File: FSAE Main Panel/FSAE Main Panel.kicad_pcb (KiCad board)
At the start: 2 copper layers, 164 x 83 mm, 244 parts, among them J1 Conn_01x08, J2 Conn_01x08, J3 Conn_01x10, J4 USB Micro B, J5 Cortex_Debug, J6 Conn_01x08, Q301 IRLML6402TRPBF, Q501 SI2308CDS-T1-GE3, Q502 SI2308CDS-T1-GE3, Q503 SI2308CDS-T1-GE3, Q504 SI2308CDS-T1-GE3, U101 SAMD21G18A-AU, U201 CD40106BPWR, U202 CD74HC238PWR, U301 TPS564201, U302 LM2940IMP-5.0/NOPB, U303 LP5907MFX-3.3, U304 LP5907MFX-3.3, U305 LP5907MFX-3.3, U401 MCP25625, U501 TLC6C598, U502 TLC6C5816, U503 TLC6C5816, Y101 32.768kHz, Y102 16MHz, Y401 16MHz

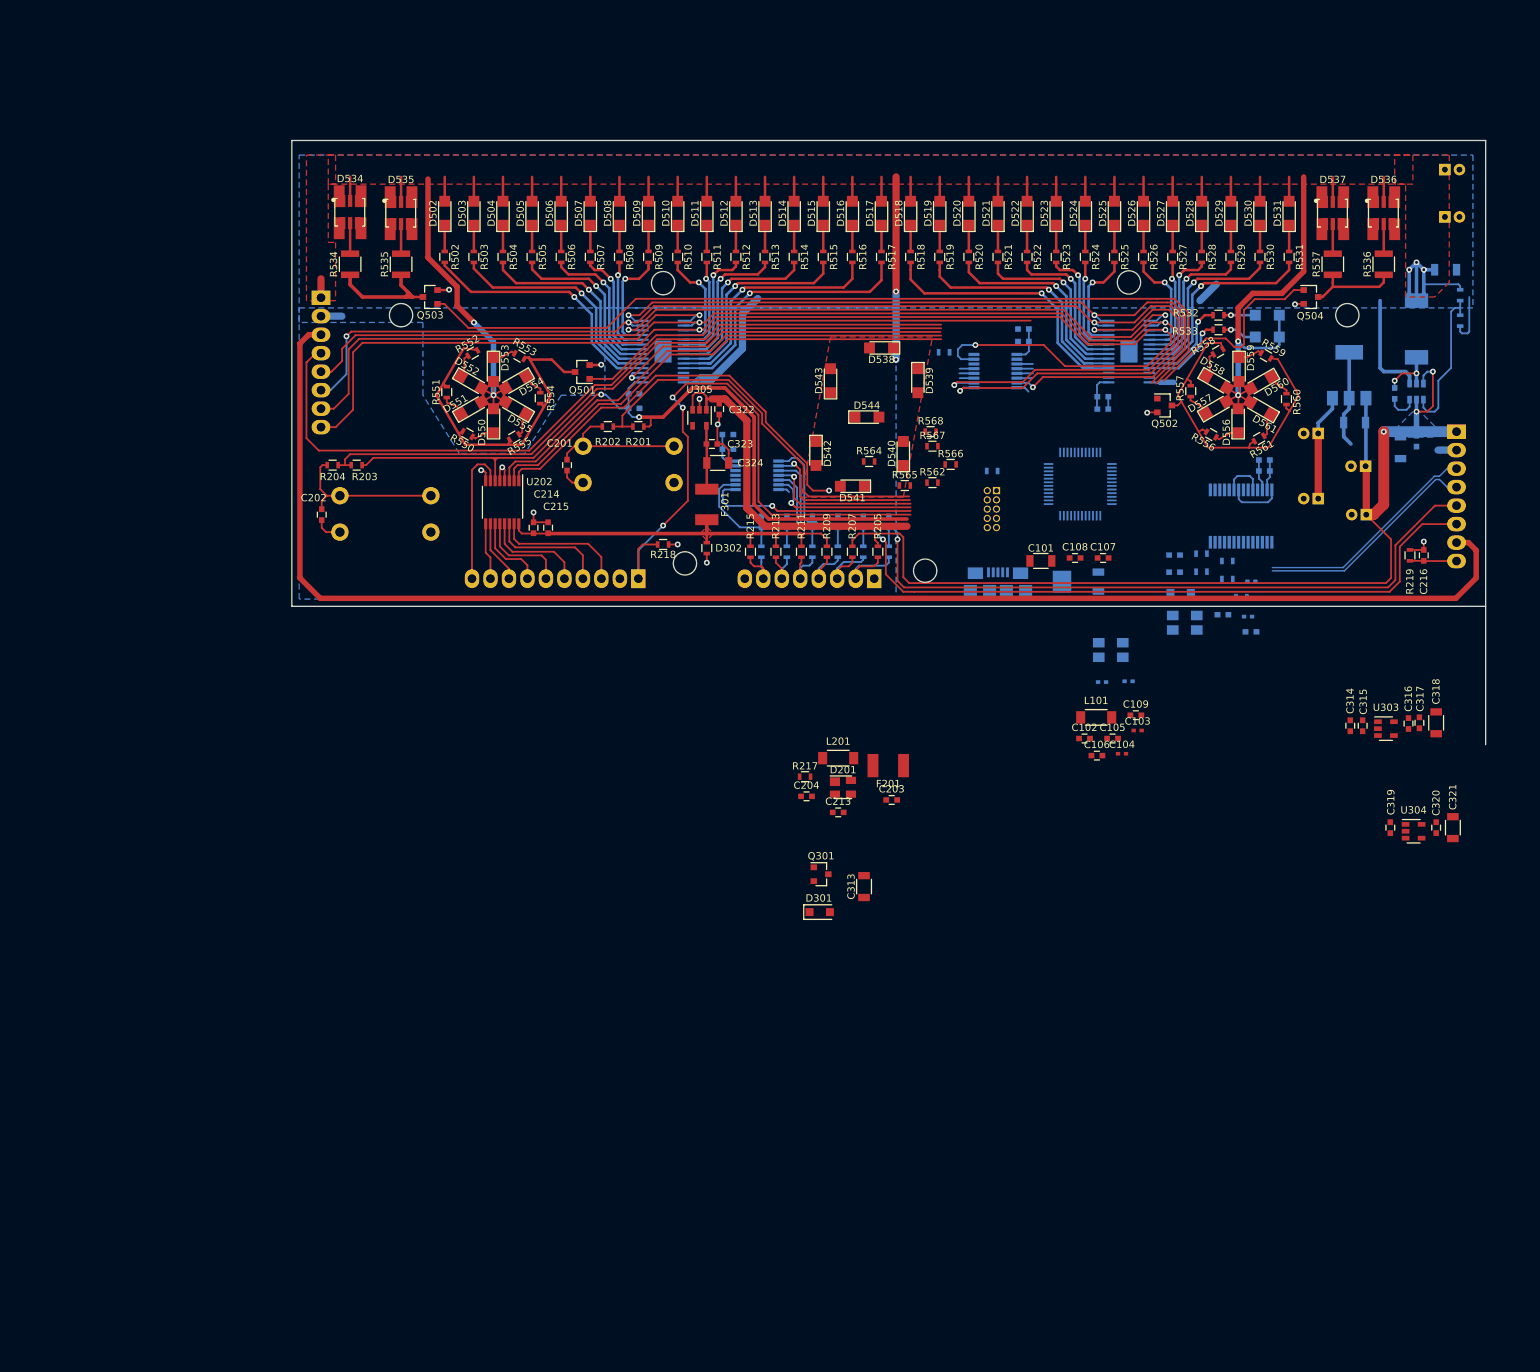
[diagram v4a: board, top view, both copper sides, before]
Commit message: Completed IO and CAN
Remaining: MCU pinning and changing the 3.3V supply locations
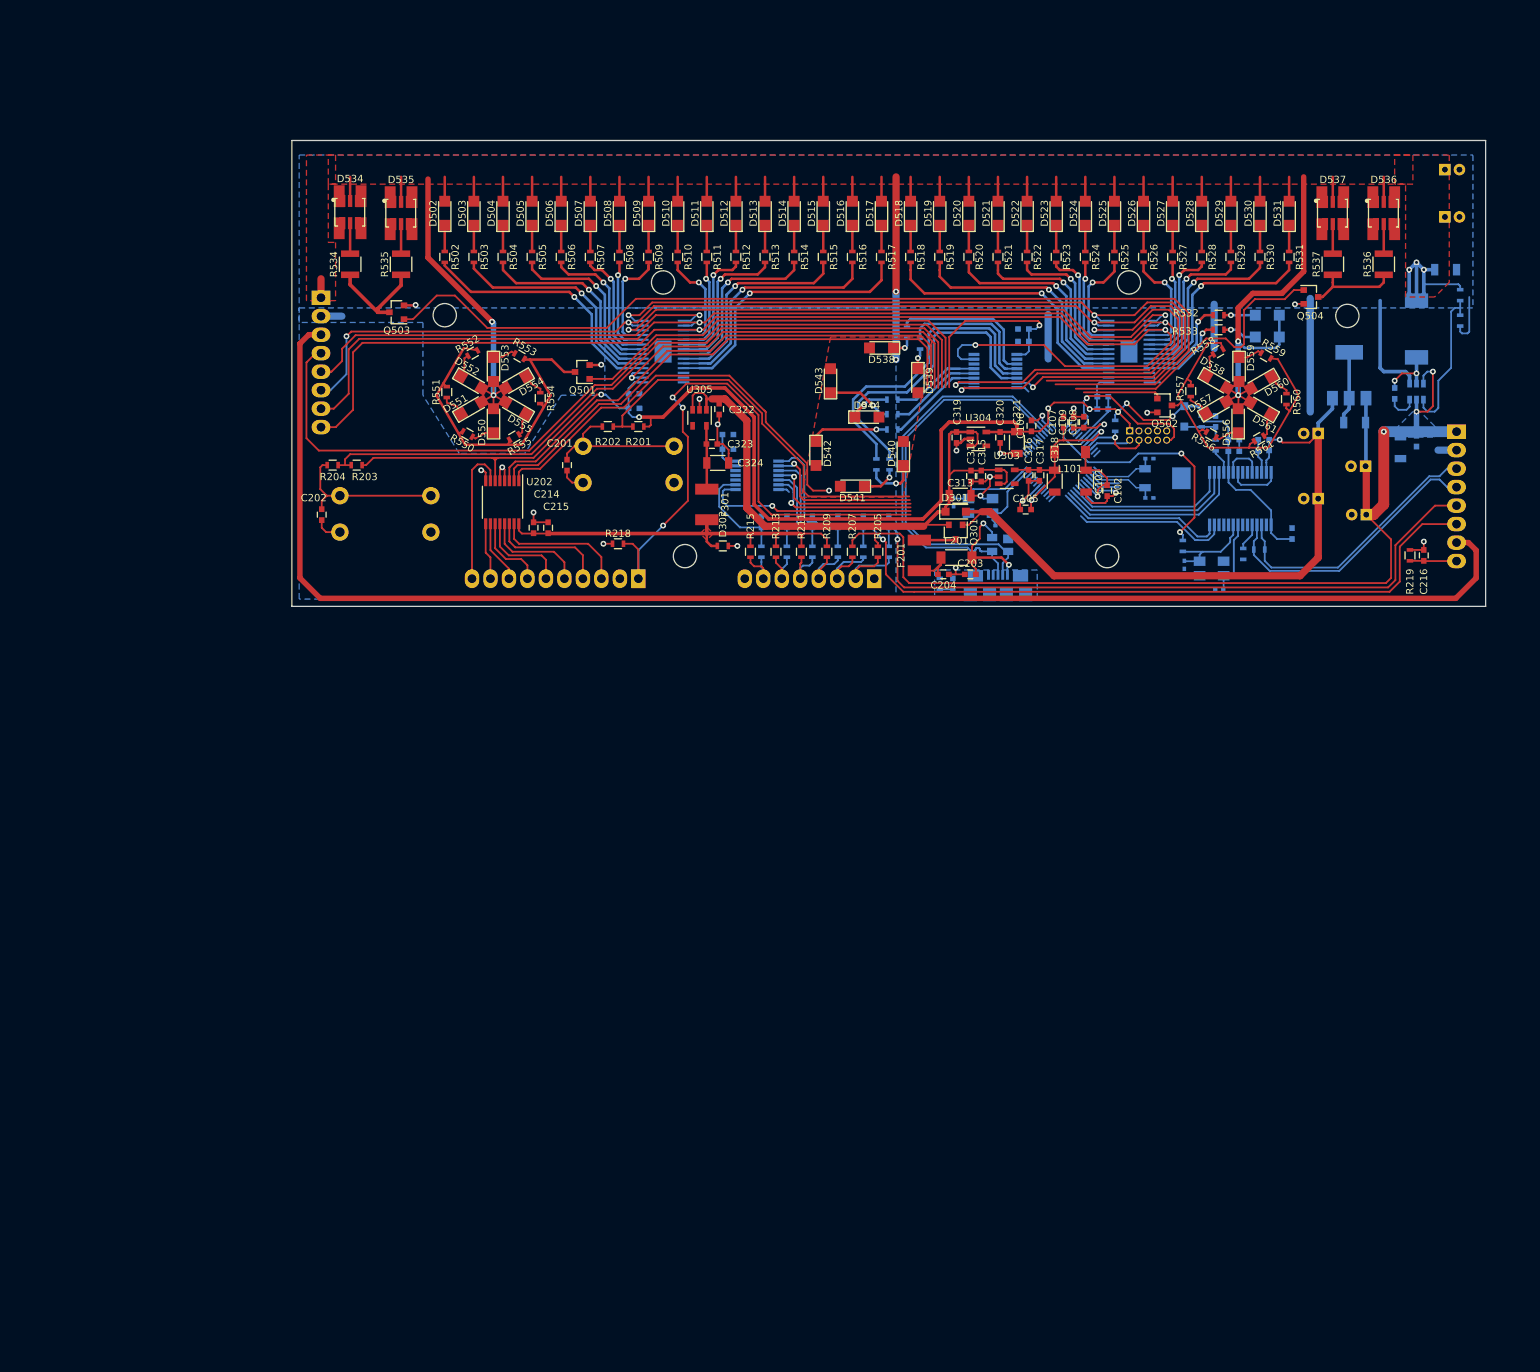
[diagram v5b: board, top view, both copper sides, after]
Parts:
- C103, C104, C213, D201, R217, R562, R564, R565, R566, R567, R568: moved to B.Cu
- moved U304 80.5 mm to (198.3, 100.0)
- moved C320 80.4 mm to (201.3, 99.8)
- moved C319 80.2 mm to (195.3, 99.8)
- moved C321 79.9 mm to (203.6, 100.5)
- moved C315 62.6 mm to (198.7, 105.1)
- moved U303 62.5 mm to (202.2, 105.2)
- moved C314 62.4 mm to (197.3, 105.1)
- moved C316 62.4 mm to (205.2, 105.0)
- moved C317 62.3 mm to (206.7, 105.0)
- moved C318 62.0 mm to (208.8, 105.8)
- moved D301 58.1 mm to (195.2, 110.0)
- moved C313 55.3 mm to (195.8, 107.8), turned to 0 degrees
- moved Q301 50.5 mm to (195.2, 112.8), turned to 270 degrees
- moved C106 46.2 mm to (205.6, 98.2), turned to 90 degrees
- moved C109 41.2 mm to (211.4, 97.7), turned to 90 degrees
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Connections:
- U502 pad : (no net) -> GND
- U503 pad : (no net) -> GND
- Y101 pad 3: (no net) -> GND
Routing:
- net +3V3: track 124.7 -> 245.0 mm, vias 2 -> 8
- net +5V: track 18.9 -> 91.3 mm, vias 0 -> 1
- net USB_D+: track 0.00 -> 54.0 mm
- net USB_D-: track 0.00 -> 54.0 mm
- net GND: track 115.6 -> 167.3 mm, vias 12 -> 21
- net /Display/cI: track 2.20 -> 43.5 mm
- net /Display/dI: track 2.15 -> 42.7 mm
- net /Power/+5V_INT: track 47.9 -> 86.5 mm
- net GCLK_0: track 0.00 -> 33.8 mm, vias 0 -> 2
- net +3.3VA: track 0.00 -> 29.6 mm, vias 0 -> 2
- net CAN_CS: track 0.00 -> 25.6 mm
- net CAN_MISO: track 0.00 -> 24.1 mm
- net CAN_SCLK: track 0.00 -> 22.9 mm
- net CAN_MOSI: track 0.00 -> 22.7 mm
- net ~RESET: track 55.2 -> 77.3 mm, vias 0 -> 1
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- added copper zone on B.Cu, net /External Interface/USB_SHLD
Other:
- board size 164 x 83 mm -> 164 x 64 mm
- board text added: "Display CL X 182.8"
- board text added: "Mounting CL X 187"
